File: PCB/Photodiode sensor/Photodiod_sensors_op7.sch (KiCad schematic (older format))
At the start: 24 parts, among them J1 Conn_01x03_Male, U1 OP07, U2 OP07, U3 OP07, U4 OP07

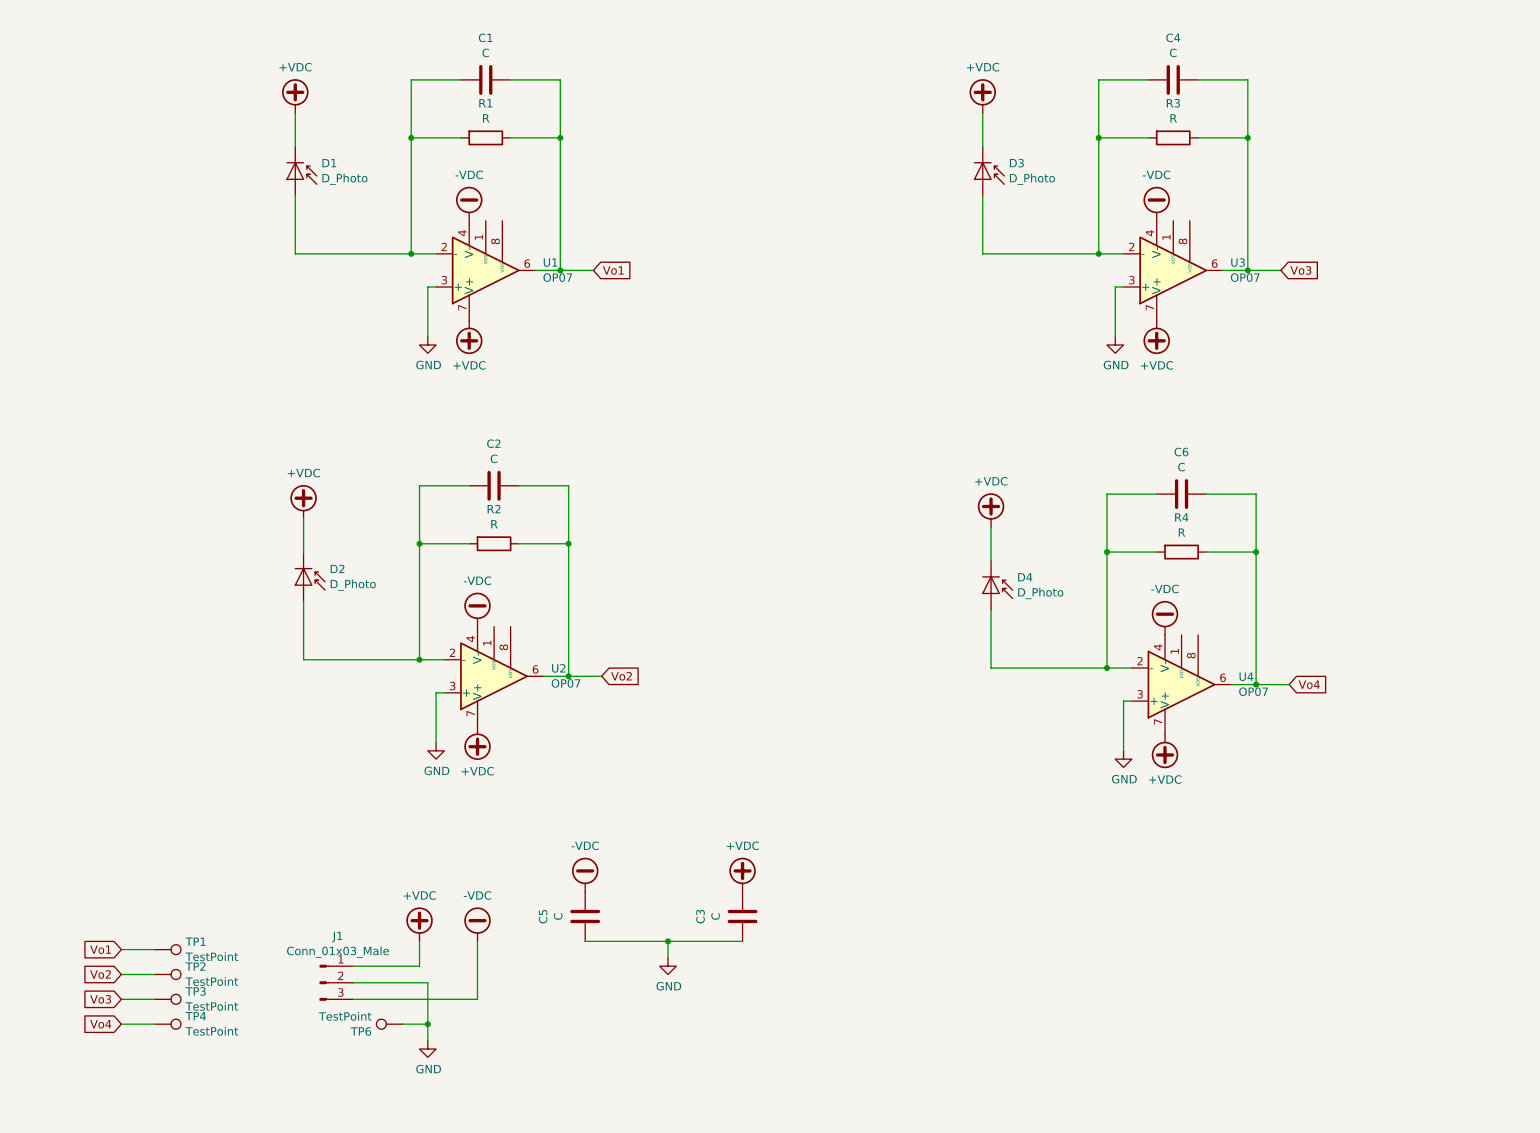
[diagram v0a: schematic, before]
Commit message: added ADC
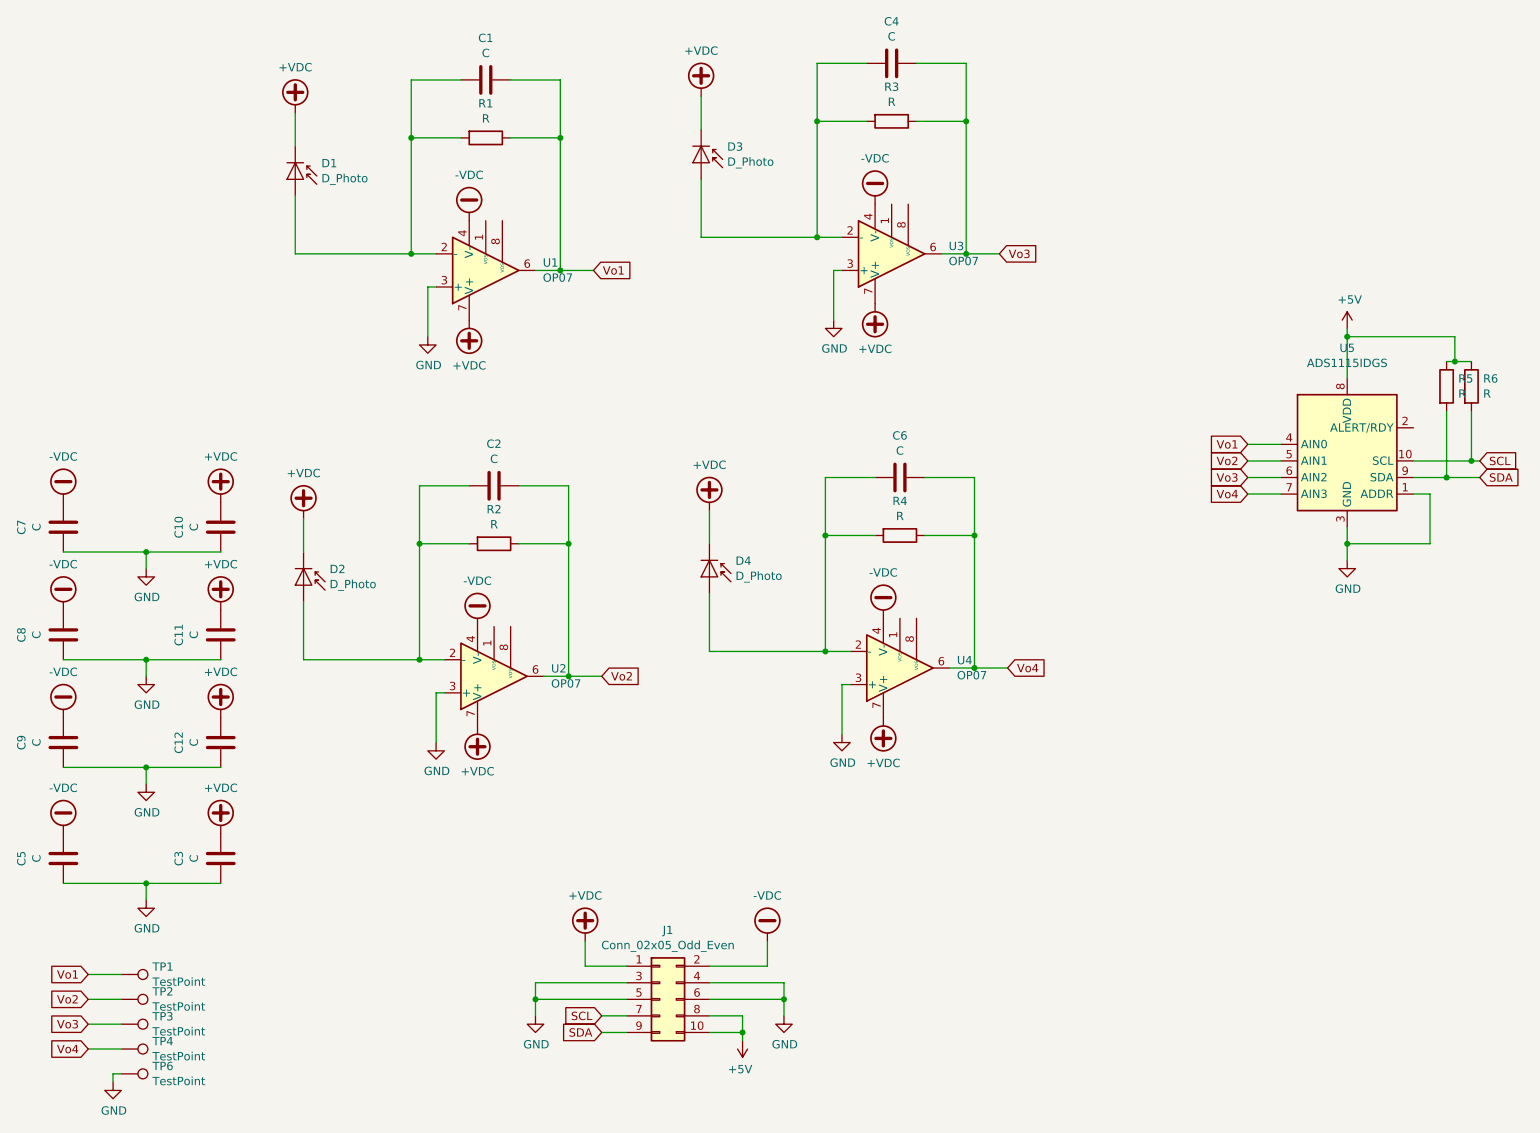
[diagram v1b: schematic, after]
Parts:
- removed J1: Conn_01x03_Male, TerminalBlock:TerminalBlock_bornier-3_P5.08mm, symbol Connector:Conn_01x03_Male
- added C10, C11, C12, C7, C8, C9: C, Capacitor_SMD:C_1206_3216Metric, symbol Device:C
- added J1: Conn_02x05_Odd_Even, Connector_IDC:IDC-Header_2x05_P2.54mm_Vertical, symbol Connector_Generic:Conn_02x05_Odd_Even
- added R5, R6: R, Resistor_SMD:R_1206_3216Metric, symbol Device:R
- added U5: ADS1115IDGS, Package_SO:TSSOP-10_3x3mm_P0.5mm, symbol Analog_ADC:ADS1115IDGS
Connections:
- net +VDC: now also C10.1, C11.1, C12.1, J1.1 (Pin_1)
- net -VDC: now also C7.1, C8.1, C9.1, J1.2 (Pin_2)
- net GND: now also C10.2, C11.2, C12.2, C7.2, C8.2, C9.2, J1.3 (Pin_3), J1.4 (Pin_4), J1.5 (Pin_5), J1.6 (Pin_6), U5.1 (ADDR), U5.3 (GND)
- net Vo1: now also U5.4 (AIN0)
- net Vo2: now also U5.5 (AIN1)
- net Vo3: now also U5.6 (AIN2)
- net Vo4: now also U5.7 (AIN3)
- new net +5V: J1.10 (Pin_10), J1.8 (Pin_8), R5.1, R6.1, U5.8 (VDD)
- new net SCL: J1.7 (Pin_7), R6.2, U5.10 (SCL)
- new net SDA: J1.9 (Pin_9), R5.2, U5.9 (SDA)
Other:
- moved on the sheet: C3, C4, C5, C6, D3, D4, R3, R4, TP1, TP2, TP3, TP4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
